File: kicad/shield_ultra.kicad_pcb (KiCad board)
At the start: 2 copper layers, 12 parts, among them J1 Ultrason, J2 IR, J3 Accel, J4 IR, J5 Ultrason, J6 IR, J7 Ultrason, J8 Ultrason, J9 Ultrason, U1 Conn_shield

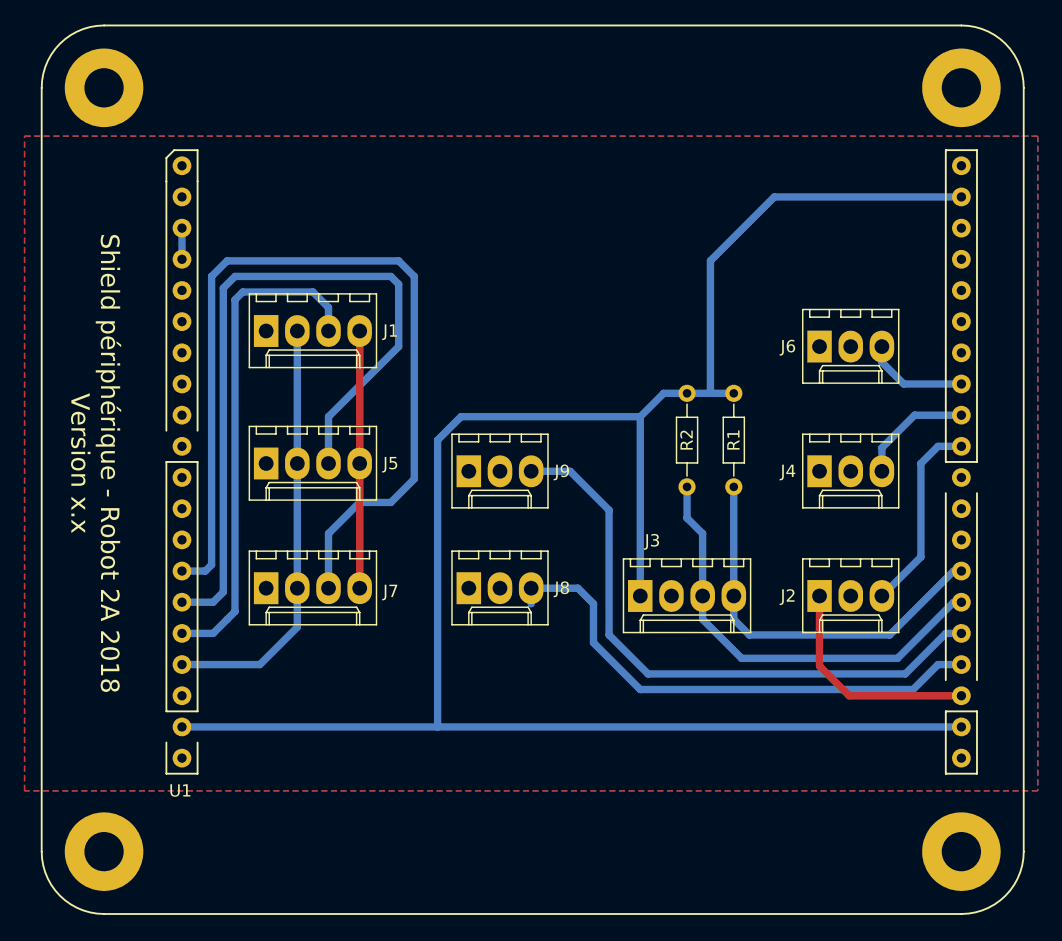
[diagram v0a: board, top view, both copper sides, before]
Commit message: Modification connexions capteurs
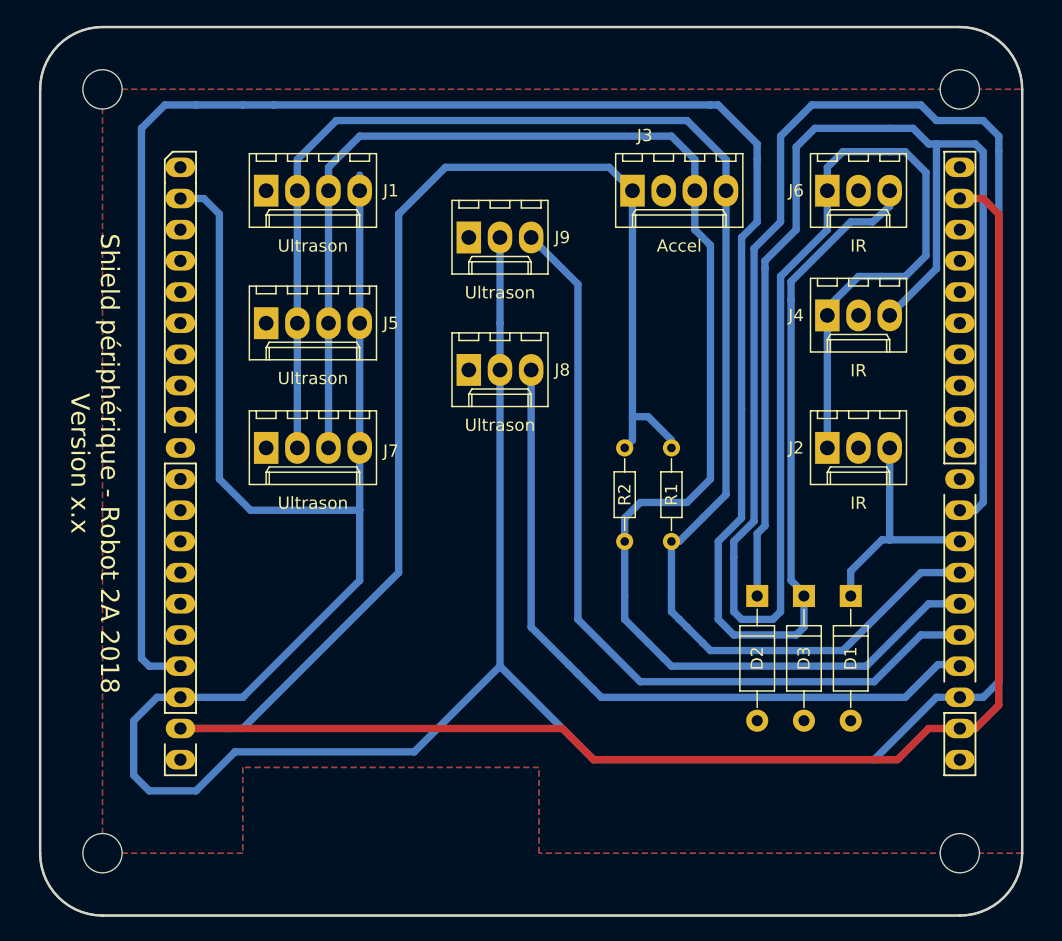
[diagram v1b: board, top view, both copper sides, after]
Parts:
- added D1: 3.3V, Diodes_THT:D_A-405_P10.16mm_Horizontal, F.Cu at (101.0, 68.6)
- added D2: 3.3V, Diodes_THT:D_A-405_P10.16mm_Horizontal, F.Cu at (93.3, 68.6)
- added D3: 3.3V, Diodes_THT:D_A-405_P10.16mm_Horizontal, F.Cu at (97.2, 68.6)
- moved J3 33.0 mm to (83.2, 35.6)
- moved J9 19.1 mm to (69.8, 39.4)
- moved J8 17.8 mm to (69.8, 50.2)
- moved J4 12.7 mm to (99.1, 45.7)
- moved J6 12.7 mm to (99.1, 35.6)
- moved J2 12.1 mm to (99.1, 56.5)
- moved J1 11.4 mm to (53.3, 35.6)
- moved J5 11.4 mm to (53.3, 46.4)
- moved J7 11.4 mm to (53.3, 56.5)
- moved R1 6.75 mm to (86.4, 56.5)
- moved R2 6.75 mm to (82.5, 56.5)
- moved U1 0.18 mm to (46.4, 81.9)
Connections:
- J1 pad 2: /B4 -> /B3
- J1 pad 3: /B5 -> /B2
- J2 pad 3: /C0 -> /A0
- J4 pad 3: /C1 -> /A1
- J5 pad 2: /B4 -> /B3
- J5 pad 3: /B6 -> /B2
- J6 pad 3: /C2 -> /B4
- J7 pad 2: /B4 -> /B3
- J7 pad 3: /B7 -> /B2
- U1 pad A0: (no net) -> /A0
- U1 pad A1: (no net) -> /A1
- U1 pad B5: /B5 -> (no net)
- U1 pad B6: /B6 -> (no net)
- U1 pad B7: /B7 -> (no net)
- U1 pad C0: /C0 -> (no net)
- U1 pad C1: /C1 -> (no net)
- U1 pad C2: /C2 -> (no net)
- U1 pad L1: Net-(U1-PadL1) -> (no net)
- U1 pad V34: Net-(U1-PadL1) -> (no net)
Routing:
- net +5V: track 39.2 -> 398.3 mm
- net /B4: track 34.8 -> 187.1 mm
- net /A1: track 0.00 -> 101.5 mm
- net /B3: track 32.0 -> 128.8 mm
- net /B2: track 35.6 -> 129.9 mm
- net /B7: track 73.5 -> 0.00 mm
- net /B6: track 60.4 -> 0.00 mm
- net +3V3: track 160.6 -> 212.8 mm
- net /B5: track 40.8 -> 0.00 mm
- net /A0: track 0.00 -> 19.6 mm
- net /B0: track 42.4 -> 60.7 mm
- net /B1: track 49.2 -> 67.5 mm
- net /C0: track 16.0 -> 0.00 mm
- net /C1: track 9.49 -> 0.00 mm
- net /C2: track 8.48 -> 0.00 mm
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- added copper zone on B.Cu, net GND
- removed copper zone on B.Cu, net +5V
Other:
- board outline added: 80 x 72.4 mm

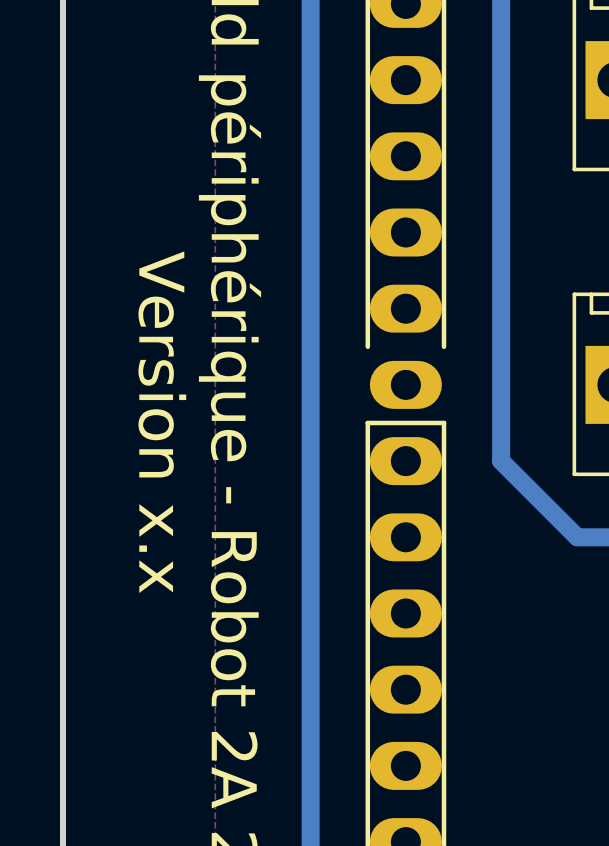
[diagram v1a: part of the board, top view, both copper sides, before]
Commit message: Mise à jour des cartouches en vue de la release
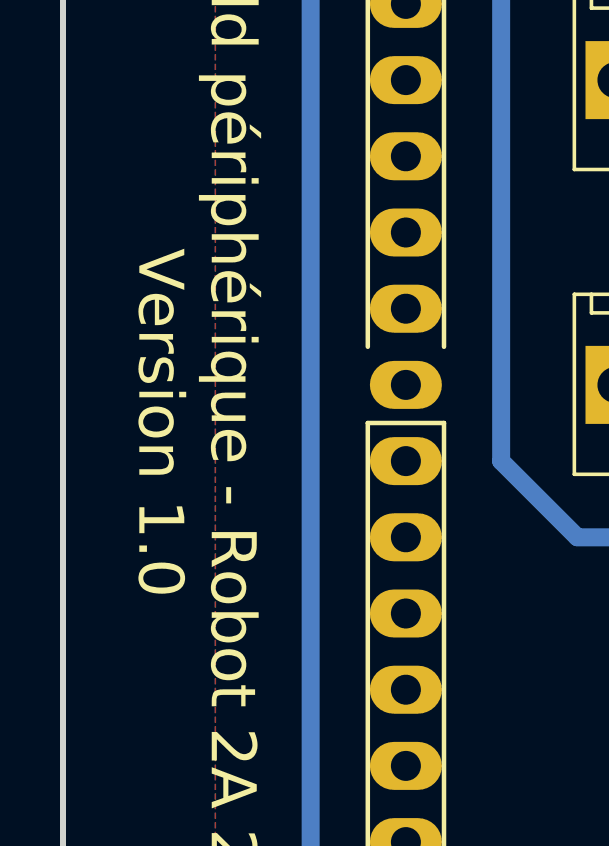
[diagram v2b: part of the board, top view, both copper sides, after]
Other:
- board text added: "Shield périphérique - Robot 2A 2018 Version 1.0"
- board text removed: "Shield périphérique - Robot 2A 2018 Version x.x"
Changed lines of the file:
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@@
   (title_block
     (title "Shield pour périphériques - Robot 2A année 2018")
-    (rev vx.x)
+    (date 2018-04-22)
+    (rev v1.0)
     (company "Centrale Lyon")
     (comment 1 "Contcter G. CHARREAUX (chxguillaume@gmail.com)")
@@
   (gr_arc (start 40.005 27.305) (end 34.925 27.305) (angle 90) (layer Edge.Cuts) (width 0.2))
   (gr_arc (start 109.855 27.305) (end 109.855 22.225) (angle 90) (layer Edge.Cuts) (width 0.2))
-  (gr_text "Shield périphérique - Robot 2A 2018\nVersion x.x" (at 39.37 57.785 270) (layer F.SilkS)
+  (gr_text "Shield périphérique - Robot 2A 2018\nVersion 1.0" (at 39.37 57.785 270) (layer F.SilkS)
     (effects (font (size 1.5 1.5) (thickness 0.3)))
   )
